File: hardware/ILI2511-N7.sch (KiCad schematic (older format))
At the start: 30 parts, among them J1 TPCON1, J2 TPCON2, J3 I2C Touch, J4 USB_C_Receptacle_USB2.0, U1 ILITEK2511, U2 AP2112K-3.3, U3 USBLC6-2SC6, Y1 12MHz

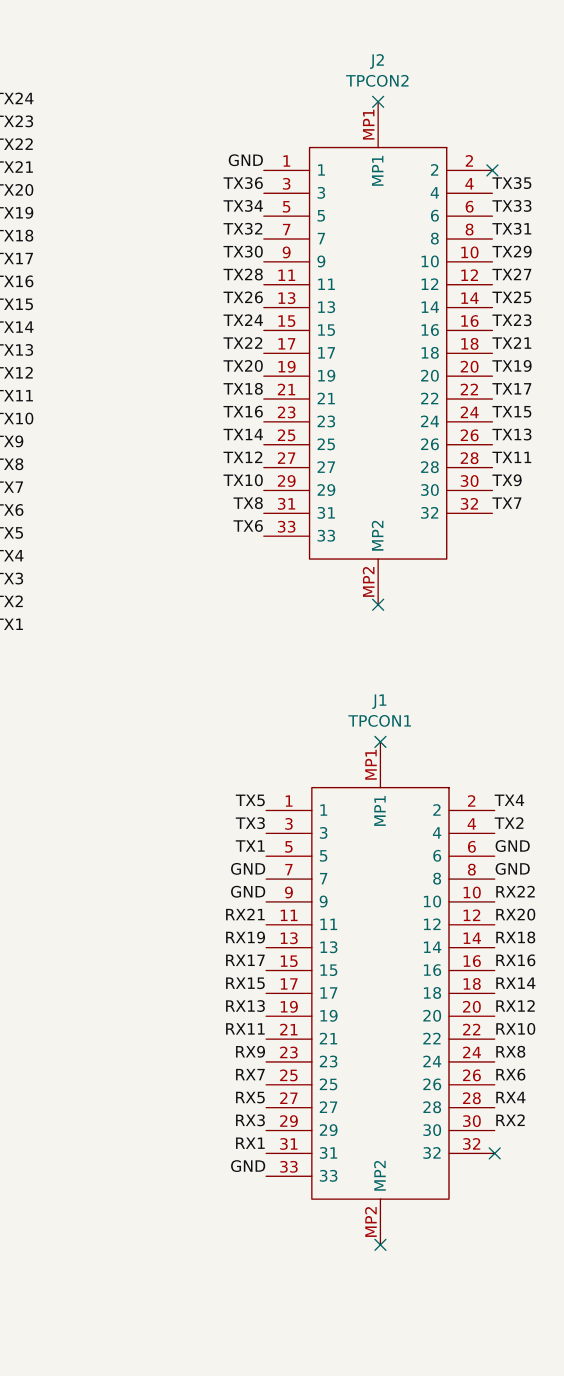
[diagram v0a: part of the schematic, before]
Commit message: added v2 with Hirose connector (as Molex was not good choice)
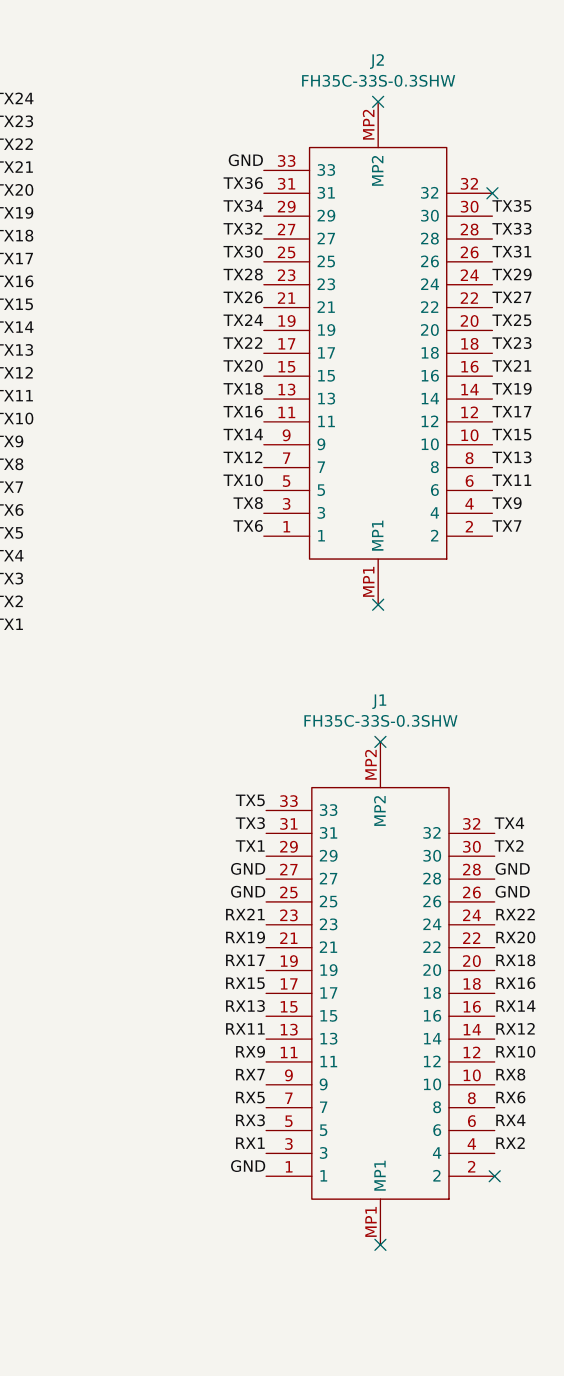
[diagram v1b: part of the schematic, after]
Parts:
- removed J1: TPCON1, Connectors_pretty:Molex-5025983393, symbol Connectors_library:Molex-502598-3393
- removed J2: TPCON2, Connectors_pretty:Molex-5025983393, symbol Connectors_library:Molex-502598-3393
- added J1, J2: FH35C-33S-0.3SHW, Connectors_pretty:FH35C33S03SHW, symbol Connectors_library:FH35C-33S-0.3SHW
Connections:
- net GND: now also J1.1, J1.25, J1.26, J1.27, J1.28, J2.33
- net RX1: now also J1.3
- net RX10: now also J1.12
- net RX11: now also J1.13
- net RX12: now also J1.14
- net RX13: now also J1.15
- net RX14: now also J1.16
- net RX15: now also J1.17
- net RX16: now also J1.18
- net RX17: now also J1.19
- net RX18: now also J1.20
- net RX19: now also J1.21
- net RX2: now also J1.4
- net RX20: now also J1.22
- net RX21: now also J1.23
- net RX22: now also J1.24
- net RX3: now also J1.5
- net RX4: now also J1.6
- net RX5: now also J1.7
- net RX6: now also J1.8
- net RX7: now also J1.9
- net RX8: now also J1.10
- net RX9: now also J1.11
- net TX1: now also J1.29
- net TX10: now also J2.5
- net TX11: now also J2.6
- net TX12: now also J2.7
- net TX13: now also J2.8
- net TX14: now also J2.9
- net TX15: now also J2.10
- net TX16: now also J2.11
- net TX17: now also J2.12
- net TX18: now also J2.13
- net TX19: now also J2.14
- net TX2: now also J1.30
- net TX20: now also J2.15
- net TX21: now also J2.16
- net TX22: now also J2.17
- net TX23: now also J2.18
- net TX24: now also J2.19
- net TX25: now also J2.20
- net TX26: now also J2.21
- net TX27: now also J2.22
- net TX28: now also J2.23
- net TX29: now also J2.24
- net TX3: now also J1.31
- net TX30: now also J2.25
- net TX31: now also J2.26
- net TX32: now also J2.27
- net TX33: now also J2.28
- net TX34: now also J2.29
- net TX35: now also J2.30
- net TX36: now also J2.31
- net TX4: now also J1.32
- net TX5: now also J1.33
- net TX6: now also J2.1
- net TX7: now also J2.2
- net TX8: now also J2.3
- net TX9: now also J2.4
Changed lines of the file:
@@
 Sheet 1 1
 Title "ILI2511-N7"
-Date "2020-11-13"
-Rev "v1"
+Date "2020-11-21"
+Rev "v2"
 Comp ""
 Comment1 ""
@@
 Comment4 ""
 $EndDescr
-$Comp
-L Connectors_library:Molex-502598-3393 J2
-U 1 1 5FA58D4F
-P 9310 1100
-F 0 "J2" V 9129 1100 50  0000 C CNN
-F 1 "TPCON2" V 9220 1100 50  0000 C CNN
-F 2 "Connectors_pretty:Molex-5025983393" H 11360 1400 50  0001 L CNN
-F 3 "" H 11360 1300 50  0001 L CNN
-F 4 "FFC & FPC Connectors 0.3 FPC Bck Flip Hsg Assy33CktEmbsTpPkg" H 11360 1200 50  0001 L CNN "Description"
-F 5 "1.63" H 11360 1100 50  0001 L CNN "Height"
-F 6 "538-502598-3393" H 11360 1000 50  0001 L CNN "Mouser Part Number"
-F 7 "https://www.mouser.co.uk/ProductDetail/Molex/502598-3393?qs=yd8XiKYcH9mqfH5%2FAxH%252BAg%3D%3D" H 11360 900 50  0001 L CNN "Mouser Price/Stock"
-F 8 "Molex" H 11360 800 50  0001 L CNN "Manufacturer_Name"
-F 9 "502598-3393" H 11360 700 50  0001 L CNN "Manufacturer_Part_Number"
-	1    9310 1100
-	0    1    1    0
-$EndComp
-$Comp
-L Connectors_library:Molex-502598-3393 J1
-U 1 1 5FA5AFCD
-P 9320 3900
-F 0 "J1" V 9139 3900 50  0000 C CNN
-F 1 "TPCON1" V 9230 3900 50  0000 C CNN
-F 2 "Connectors_pretty:Molex-5025983393" H 11370 4200 50  0001 L CNN
-F 3 "" H 11370 4100 50  0001 L CNN
-F 4 "FFC & FPC Connectors 0.3 FPC Bck Flip Hsg Assy33CktEmbsTpPkg" H 11370 4000 50  0001 L CNN "Description"
-F 5 "1.63" H 11370 3900 50  0001 L CNN "Height"
-F 6 "538-502598-3393" H 11370 3800 50  0001 L CNN "Mouser Part Number"
-F 7 "https://www.mouser.co.uk/ProductDetail/Molex/502598-3393?qs=yd8XiKYcH9mqfH5%2FAxH%252BAg%3D%3D" H 11370 3700 50  0001 L CNN "Mouser Price/Stock"
-F 8 "Molex" H 11370 3600 50  0001 L CNN "Manufacturer_Name"
-F 9 "502598-3393" H 11370 3500 50  0001 L CNN "Manufacturer_Part_Number"
-	1    9320 3900
-	0    1    1    0
-$EndComp
 $Comp
 L IC_library:ILITEK2511 U1
@@
 Text Label 8820 4500 2    50   ~ 0
 GND
+Text Label 9820 4600 0    50   ~ 0
+GND
 Text Label 9820 4500 0    50   ~ 0
 GND
-Text Label 9820 4400 0    50   ~ 0
-GND
-NoConn ~ 9820 5700
-NoConn ~ 9810 1400
+NoConn ~ 9820 5800
+NoConn ~ 9810 1500
 Text Label 8810 1400 2    50   ~ 0
 GND
@@
 Text Label 8810 2000 2    50   ~ 0
 TX26
-Text Label 9810 1500 0    50   ~ 0
+Text Label 9810 1600 0    50   ~ 0
 TX35
-Text Label 9810 1600 0    50   ~ 0
+Text Label 9810 1700 0    50   ~ 0
 TX33
-Text Label 9810 1700 0    50   ~ 0
+Text Label 9810 1800 0    50   ~ 0
 TX31
-Text Label 9810 1800 0    50   ~ 0
+Text Label 9810 1900 0    50   ~ 0
 TX29
-Text Label 9810 1900 0    50   ~ 0
+Text Label 9810 2000 0    50   ~ 0
 TX27
-Text Label 9810 2000 0    50   ~ 0
+Text Label 9810 2100 0    50   ~ 0
 TX25
-Text Label 9810 2100 0    50   ~ 0
+Text Label 9810 2200 0    50   ~ 0
 TX23
-Text Label 9810 2200 0    50   ~ 0
+Text Label 9810 2300 0    50   ~ 0
 TX21
-Text Label 9810 2300 0    50   ~ 0
+Text Label 9810 2400 0    50   ~ 0
 TX19
-Text Label 9810 2400 0    50   ~ 0
+Text Label 9810 2500 0    50   ~ 0
 TX17
-Text Label 9810 2500 0    50   ~ 0
+Text Label 9810 2600 0    50   ~ 0
 TX15
-Text Label 9810 2600 0    50   ~ 0
+Text Label 9810 2700 0    50   ~ 0
 TX13
-Text Label 9810 2700 0    50   ~ 0
+Text Label 9810 2800 0    50   ~ 0
 TX11
-Text Label 9810 2800 0    50   ~ 0
+Text Label 9810 2900 0    50   ~ 0
 TX9
-Text Label 9810 2900 0    50   ~ 0
+Text Label 9810 3000 0    50   ~ 0
 TX7
 Text Label 8810 2100 2    50   ~ 0
@@
 Text Label 8810 3000 2    50   ~ 0
 TX6
-Text Label 9820 4200 0    50   ~ 0
+Text Label 9820 4300 0    50   ~ 0
 TX4
-Text Label 9820 4300 0    50   ~ 0
+Text Label 9820 4400 0    50   ~ 0
 TX2
 Text Label 8820 4200 2    50   ~ 0
@@
 Text Label 8820 5700 2    50   ~ 0
 RX1
+Text Label 9820 5700 0    50   ~ 0
+RX2
 Text Label 9820 5600 0    50   ~ 0
-RX2
+RX4
 Text Label 9820 5500 0    50   ~ 0
-RX4
+RX6
 Text Label 9820 5400 0    50   ~ 0
-RX6
+RX8
 Text Label 9820 5300 0    50   ~ 0
-RX8
+RX10
 Text Label 9820 5200 0    50   ~ 0
-RX10
+RX12
 Text Label 9820 5100 0    50   ~ 0
-RX12
+RX14
 Text Label 9820 5000 0    50   ~ 0
-RX14
+RX16
 Text Label 9820 4900 0    50   ~ 0
-RX16
+RX18
 Text Label 9820 4800 0    50   ~ 0
-RX18
+RX20
 Text Label 9820 4700 0    50   ~ 0
-RX20
-Text Label 9820 4600 0    50   ~ 0
 RX22
 Text Label 8820 4700 2    50   ~ 0
@@
 Text Label 6360 2100 0    50   ~ 0
 TX36
+$Comp
+L Connectors_library:FH35C-33S-0.3SHW J2
+U 1 1 5FB8A692
+P 9310 3300
+F 0 "J2" V 11691 3300 50  0000 C CNN
+F 1 "FH35C-33S-0.3SHW" V 11600 3300 50  0000 C CNN
+F 2 "Connectors_pretty:FH35C33S03SHW" H 11360 3600 50  0001 L CNN
+F 3 "https://www.hirose.com/product/download/?distributor=digikey&type=2d&lang=en&num=FH35C-33S-0.3SHW(99)" H 11360 3500 50  0001 L CNN
+F 4 "FFC & FPC Connectors 33P BCKFLP DUAL-SIDE FPC 0.3mm P 0.9mm H" H 11360 3400 50  0001 L CNN "Description"
+F 5 "1.8" H 11360 3300 50  0001 L CNN "Height"
+F 6 "798-FH35C33S03SHW99" H 11360 3200 50  0001 L CNN "Mouser Part Number"
+F 7 "https://www.mouser.co.uk/ProductDetail/Hirose-Connector/FH35C-33S-03SHW99?qs=zPSbg0dgZogDeOtaYQV5yA%3D%3D" H 11360 3100 50  0001 L CNN "Mouser Price/Stock"
+F 8 "Hirose" H 11360 3000 50  0001 L CNN "Manufacturer_Name"
+F 9 "FH35C-33S-0.3SHW(99)" H 11360 2900 50  0001 L CNN "Manufacturer_Part_Number"
+	1    9310 3300
+	0    1    -1   0
+$EndComp
+$Comp
+L Connectors_library:FH35C-33S-0.3SHW J1
+U 1 1 5FBA4832
+P 9320 6100
+F 0 "J1" V 11701 6100 50  0000 C CNN
+F 1 "FH35C-33S-0.3SHW" V 11610 6100 50  0000 C CNN
+F 2 "Connectors_pretty:FH35C33S03SHW" H 11370 6400 50  0001 L CNN
+F 3 "https://www.hirose.com/product/download/?distributor=digikey&type=2d&lang=en&num=FH35C-33S-0.3SHW(99)" H 11370 6300 50  0001 L CNN
+F 4 "FFC & FPC Connectors 33P BCKFLP DUAL-SIDE FPC 0.3mm P 0.9mm H" H 11370 6200 50  0001 L CNN "Description"
+F 5 "1.8" H 11370 6100 50  0001 L CNN "Height"
+F 6 "798-FH35C33S03SHW99" H 11370 6000 50  0001 L CNN "Mouser Part Number"
+F 7 "https://www.mouser.co.uk/ProductDetail/Hirose-Connector/FH35C-33S-03SHW99?qs=zPSbg0dgZogDeOtaYQV5yA%3D%3D" H 11370 5900 50  0001 L CNN "Mouser Price/Stock"
+F 8 "Hirose" H 11370 5800 50  0001 L CNN "Manufacturer_Name"
+F 9 "FH35C-33S-0.3SHW(99)" H 11370 5700 50  0001 L CNN "Manufacturer_Part_Number"
+	1    9320 6100
+	0    1    -1   0
+$EndComp
 $EndSCHEMATC
